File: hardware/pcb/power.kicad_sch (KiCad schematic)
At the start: 40 parts, among them J1 USB-C Port B, J2 USB-C Port A, U1 USBLC6-2SC6, U2 USBLC6-2SC6, U3 TPS2121RUX, U4 TPS22965DSG, U5 XC6206P332MR

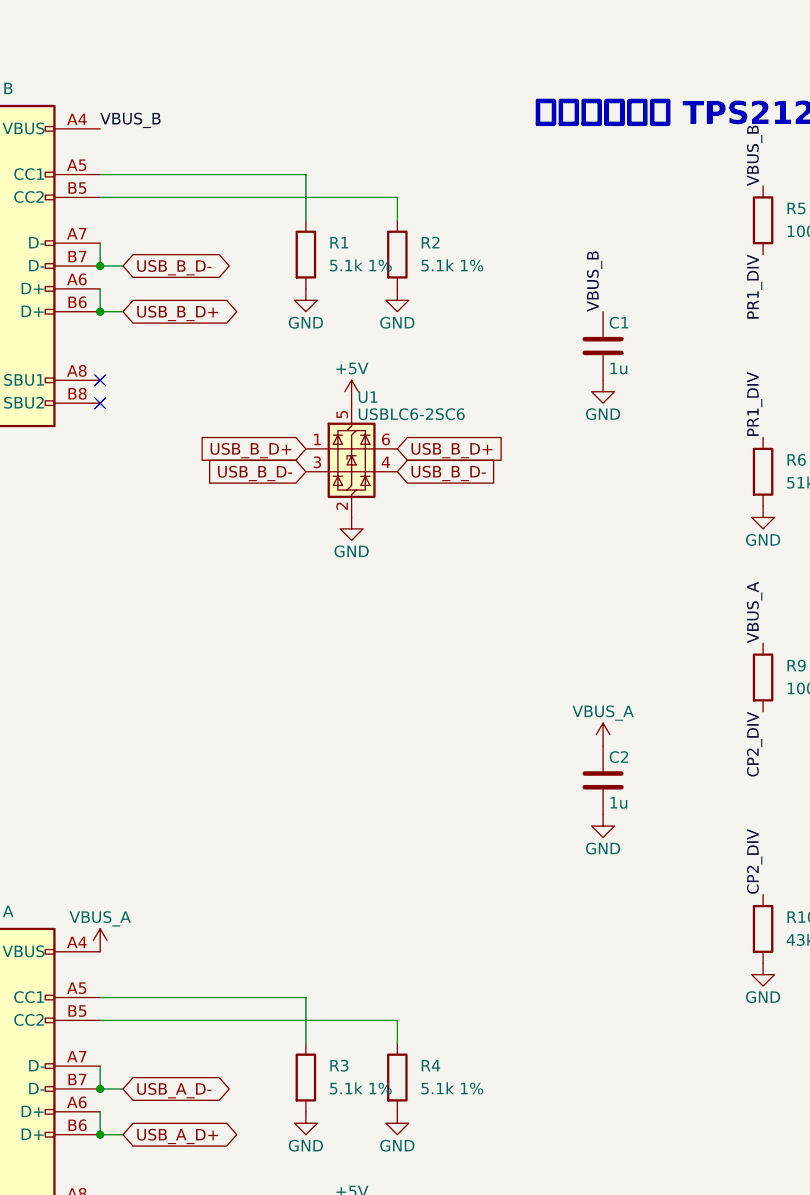
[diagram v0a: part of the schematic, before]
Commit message: Add 42-key matrix sheet, layout, and USB-C part
- Key layout from Smidr (KLE format, 42 keys) in hardware/layout,
  with the 7x6 COL2ROW matrix mapping proven on the blad keyboard
- Keymatrix sheet: 42 Choc hotswap switches and 1N4148W diodes
  (C81598, Basic), every pin labeled; RP2040 ROW/COL nets are now
  global labels, GPIO13/14 freed as spares
- USB-C receptacles J1/J2 set to HRO TYPE-C-31-M-12 (C165948)
- Power sheet: CC lines reach the RP2040 ADC again
- Docs: design decisions, pin assignment, keymatrix spec and
  reference, open items

Full project netlist matches all 141 intended nets; ERC has no errors.

Co-Authored-By: Claude Opus 5.5 <noreply@anthropic.com>
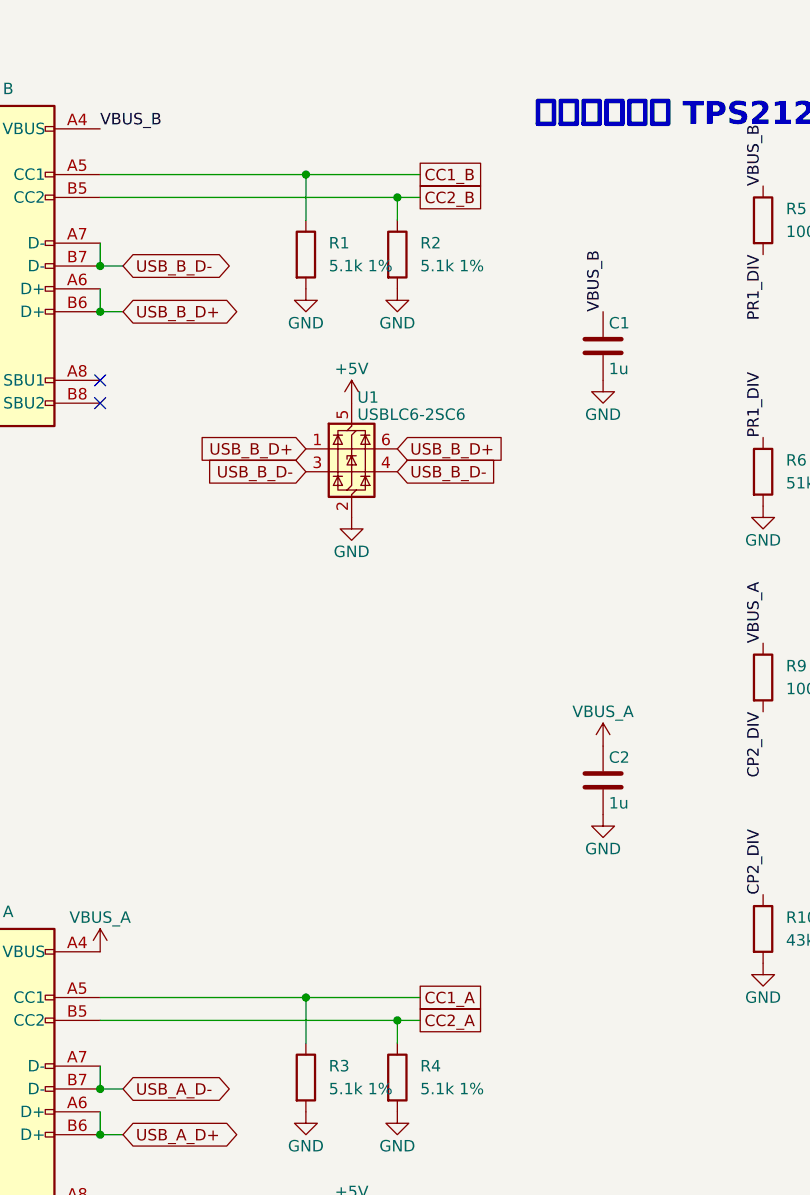
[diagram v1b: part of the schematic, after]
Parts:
- J1, J2: footprint (none) -> Connector_USB:USB_C_Receptacle_HRO_TYPE-C-31-M-12; LCSC (none) -> C165948
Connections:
- net CC2_A: now reaches J2.B5 (CC2), R4.1
- net CC1_B: now reaches J1.A5 (CC1), R1.1
- net CC2_B: now reaches J1.B5 (CC2), R2.1
- net CC1_A: now reaches J2.A5 (CC1), R3.1
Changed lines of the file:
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@@
 	)
 	(junction
+		(at 86.36 66.04)
+		(diameter 0)
+		(color 0 0 0 0)
+	)
+	(junction
 		(at 38.1 96.52)
 		(diameter 0)
@@
 	)
 	(junction
+		(at 86.36 157.48)
+		(diameter 0)
+		(color 0 0 0 0)
+	)
+	(junction
 		(at 53.34 78.74)
 		(diameter 0)
@@
 	)
 	(junction
+		(at 76.2 63.5)
+		(diameter 0)
+		(color 0 0 0 0)
+	)
+	(junction
+		(at 76.2 154.94)
+		(diameter 0)
+		(color 0 0 0 0)
+	)
+	(junction
 		(at 53.34 170.18)
 		(diameter 0)
@@
 	(wire
 		(pts
+			(xy 86.36 66.04) (xy 88.9 66.04)
+		)
+		(stroke
+			(width 0)
+			(type default)
+		)
+	)
+	(wire
+		(pts
+			(xy 76.2 63.5) (xy 88.9 63.5)
+		)
+		(stroke
+			(width 0)
+			(type default)
+		)
+	)
+	(wire
+		(pts
 			(xy 53.34 157.48) (xy 86.36 157.48)
 		)
@@
 	(wire
 		(pts
+			(xy 76.2 154.94) (xy 88.9 154.94)
+		)
+		(stroke
+			(width 0)
+			(type default)
+		)
+	)
+	(wire
+		(pts
 			(xy 53.34 63.5) (xy 76.2 63.5)
 		)
@@
 	(wire
 		(pts
+			(xy 86.36 157.48) (xy 88.9 157.48)
+		)
+		(stroke
+			(width 0)
+			(type default)
+		)
+	)
+	(wire
+		(pts
 			(xy 53.34 66.04) (xy 86.36 66.04)
 		)
@@
 		)
 	)
+	(global_label "CC1_B"
+		(shape passive)
+		(at 88.9 63.5 0)
+		(fields_autoplaced yes)
+		(effects
+			(font
+				(size 1.27 1.27)
+			)
+			(justify left)
+		)
+		(property "Intersheetrefs" "${INTERSHEET_REFS}"
+			(at 96.761 63.5 0)
+			(hide yes)
+			(show_name no)
+			(do_not_autoplace no)
+			(effects
+				(font
+					(size 1.27 1.27)
+				)
+				(justify left)
+			)
+		)
+	)
 	(global_label "USB_B_D+"
 		(shape input)
@@
 		)
 	)
+	(global_label "CC2_B"
+		(shape passive)
+		(at 88.9 66.04 0)
+		(fields_autoplaced yes)
+		(effects
+			(font
+				(size 1.27 1.27)
+			)
+			(justify left)
+		)
+		(property "Intersheetrefs" "${INTERSHEET_REFS}"
+			(at 96.761 66.04 0)
+			(hide yes)
+			(show_name no)
+			(do_not_autoplace no)
+			(effects
+				(font
+					(size 1.27 1.27)
+				)
+				(justify left)
+			)
+		)
+	)
 	(global_label "USB_A_D+"
 		(shape bidirectional)
@@
 		)
 	)
+	(global_label "CC2_A"
+		(shape passive)
+		(at 88.9 157.48 0)
+		(fields_autoplaced yes)
+		(effects
+			(font
+				(size 1.27 1.27)
+			)
+			(justify left)
+		)
+		(property "Intersheetrefs" "${INTERSHEET_REFS}"
+			(at 96.5796 157.48 0)
+			(hide yes)
+			(show_name no)
+			(do_not_autoplace no)
+			(effects
+				(font
+					(size 1.27 1.27)
+				)
+				(justify left)
+			)
+		)
+	)
 	(global_label "USB_A_D-"
 		(shape input)
@@
 		)
 	)
+	(global_label "CC1_A"
+		(shape passive)
+		(at 88.9 154.94 0)
+		(fields_autoplaced yes)
+		(effects
+			(font
+				(size 1.27 1.27)
+			)
+			(justify left)
+		)
+		(property "Intersheetrefs" "${INTERSHEET_REFS}"
+			(at 96.5796 154.94 0)
+			(hide yes)
+			(show_name no)
+			(do_not_autoplace no)
+			(effects
+				(font
+					(size 1.27 1.27)
+				)
+				(justify left)
+			)
+		)
+	)
 	(global_label "+5V_LCD"
 		(shape passive)
@@
 			)
 		)
-		(property "Footprint" ""
+		(property "Footprint" "Connector_USB:USB_C_Receptacle_HRO_TYPE-C-31-M-12"
 			(at 41.91 73.66 0)
 			(hide yes)
@@
 			)
 		)
+		(property "LCSC" "C165948"
+			(at 41.91 73.66 0)
+			(hide yes)
+			(show_name no)
+			(do_not_autoplace no)
+			(effects
+				(font
+					(size 1.27 1.27)
+				)
+			)
+		)
 		(pin "A1"
 		)
@@
 			)
 		)
-		(property "Footprint" ""
+		(property "Footprint" "Connector_USB:USB_C_Receptacle_HRO_TYPE-C-31-M-12"
 			(at 41.91 165.1 0)
 			(hide yes)
@@
 			(hide yes)
 			(show_name no)
+			(do_not_autoplace no)
+			(effects
+				(font
+					(size 1.27 1.27)
+				)
+			)
+		)
+		(property "LCSC" "C165948"
+			(at 41.91 165.1 0)
+			(hide yes)
+			(show_name no)

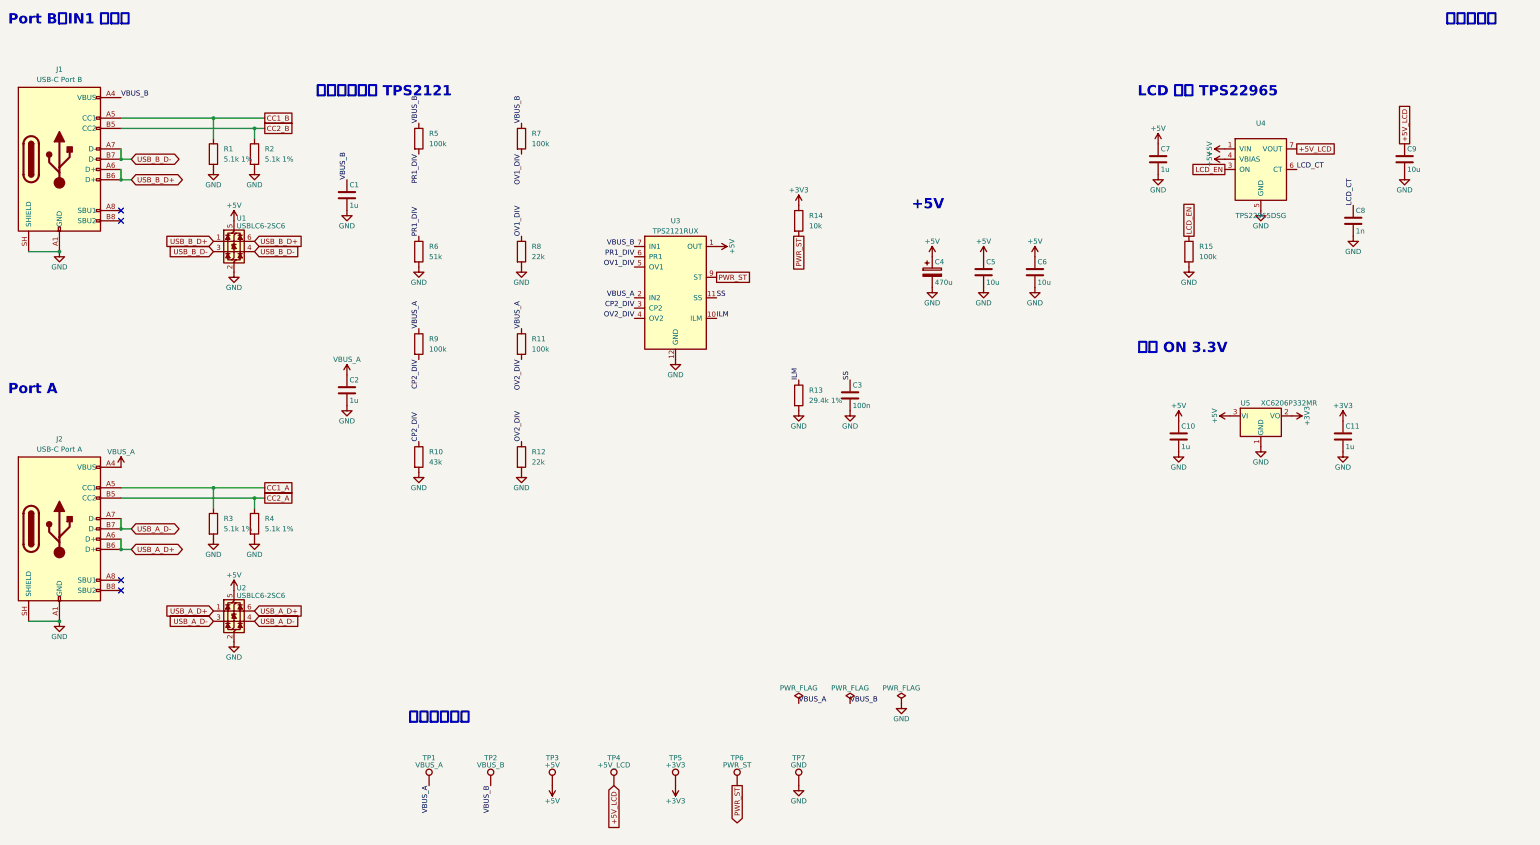
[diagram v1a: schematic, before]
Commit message: Wire the power sheet and use power symbols for +5V_LCD
Replace the labels on the power sheet with wires, use power symbols for
+5V_LCD and the VBUS test pads, and change J302 to Conn_01x03_Pin.

Co-Authored-By: Claude Opus 5.5 <noreply@anthropic.com>
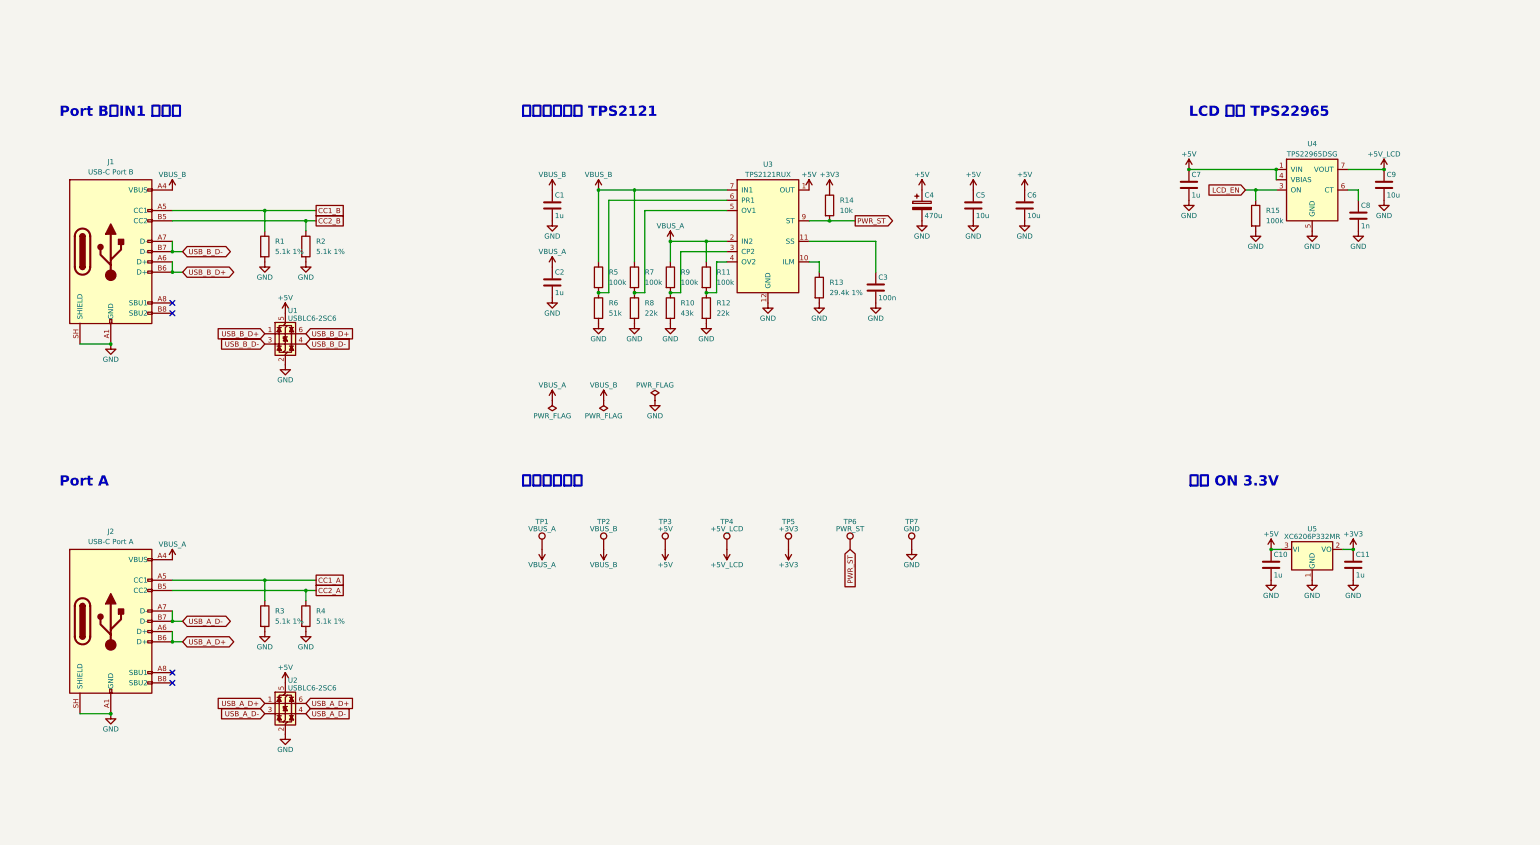
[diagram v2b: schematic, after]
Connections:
- net CP2_DIV: no longer names the net of R10.1, R9.2, U3.3 (CP2)
- net ILM: no longer names the net of R13.1, U3.10 (ILM)
- net LCD_CT: no longer names the net of C8.1, U4.6 (CT)
- net OV1_DIV: no longer names the net of R7.2, R8.1, U3.5 (OV1)
- net OV2_DIV: no longer names the net of R11.2, R12.1, U3.4 (OV2)
- net PR1_DIV: no longer names the net of R5.2, R6.1, U3.6 (PR1)
- net SS: no longer names the net of C3.1, U3.11 (SS)
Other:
- note removed: "+5V"
- note removed: "シート外へ"
- moved on the sheet: C1, C10, C11, C2, C3, C4, C5, C6, C7, C8, C9, J1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

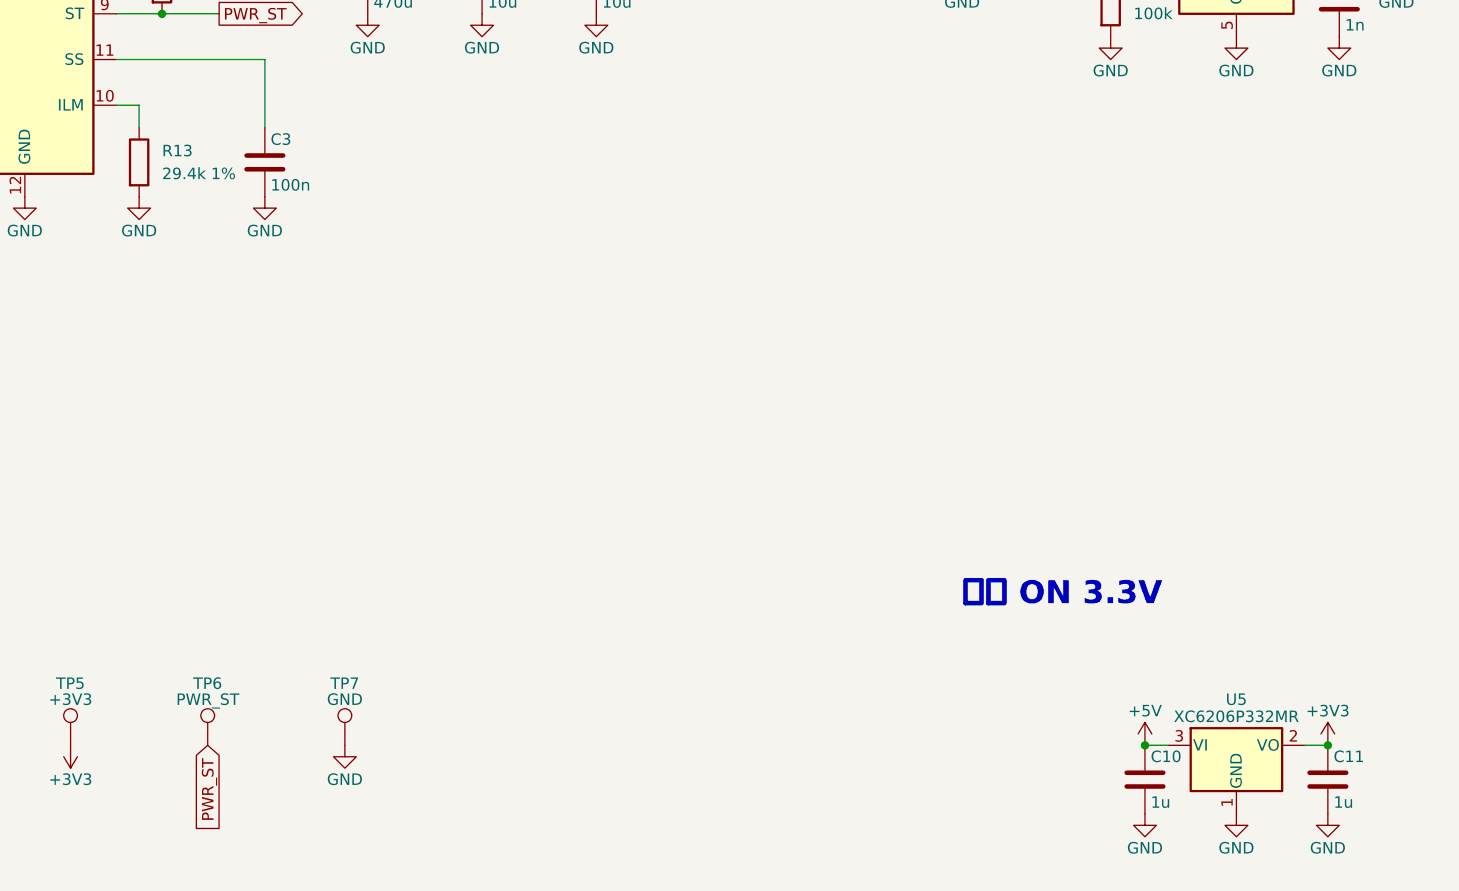
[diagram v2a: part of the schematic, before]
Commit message: Assign 0603 parts, use 30k for ILM, and switch the LDO to AP2127
Give every resistor and capacitor a 0603 footprint and an LCSC number
(Basic where possible), change the ILM resistor to a 30k Basic part,
and replace the XC6206 with an AP2127N-3.3 from stock. Record the
decisions and drop the resolved open items.

Co-Authored-By: Claude Opus 5.5 <noreply@anthropic.com>
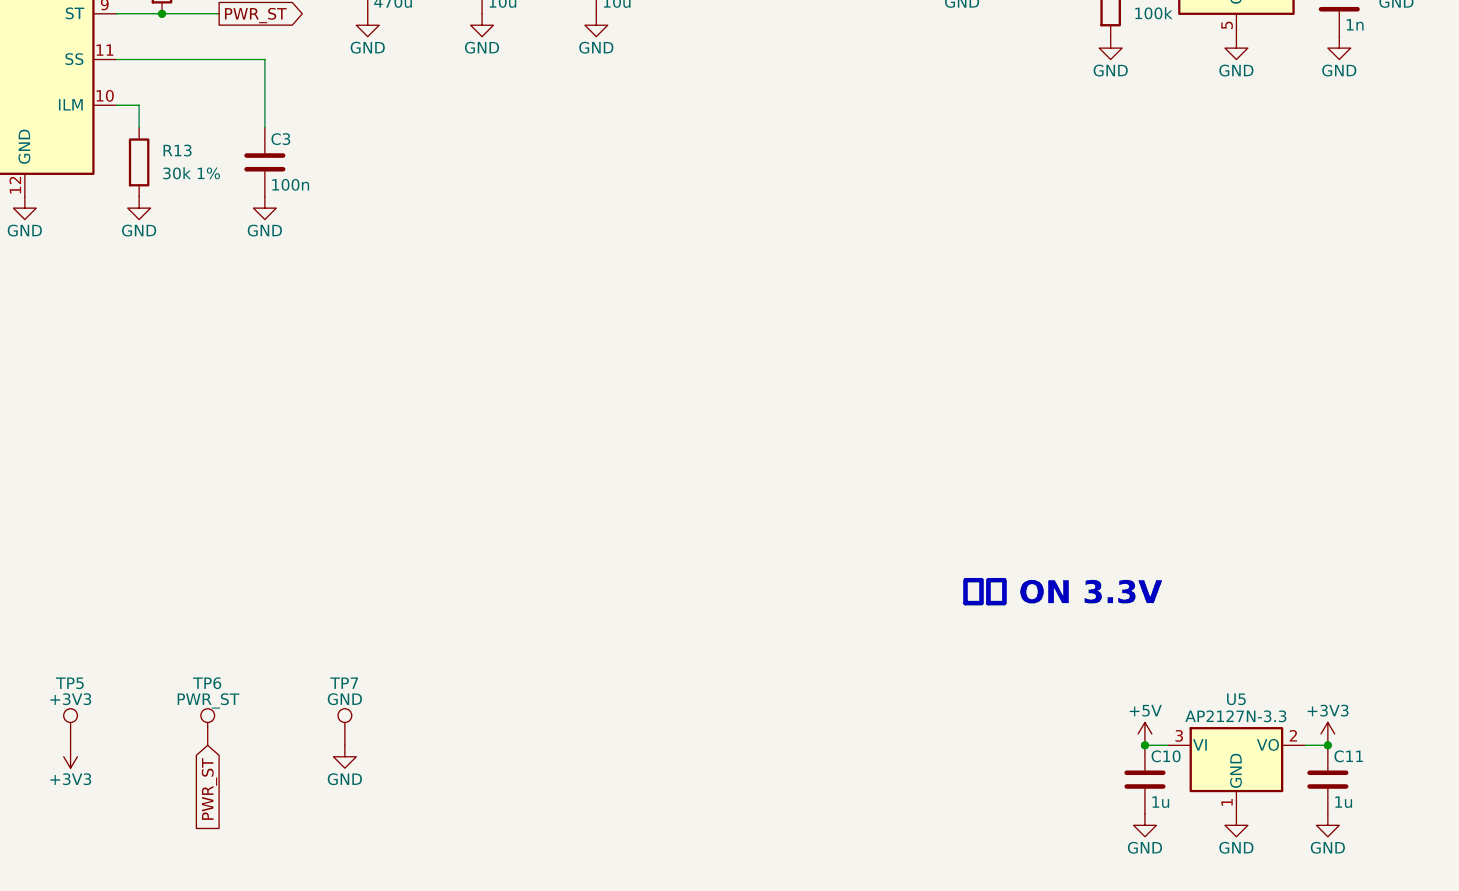
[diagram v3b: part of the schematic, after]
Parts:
- C1, C10, C11, C2, C7: footprint (none) -> Capacitor_SMD:C_0603_1608Metric; LCSC (none) -> C15849
- C3: footprint (none) -> Capacitor_SMD:C_0603_1608Metric; LCSC (none) -> C14663
- C5, C6, C9: footprint (none) -> Capacitor_SMD:C_0603_1608Metric; LCSC (none) -> C96446
- C8: footprint (none) -> Capacitor_SMD:C_0603_1608Metric; LCSC (none) -> C1588
- R1, R2, R3, R4: footprint (none) -> Resistor_SMD:R_0603_1608Metric; LCSC (none) -> C23186
- R10: footprint (none) -> Resistor_SMD:R_0603_1608Metric; LCSC (none) -> C23172
- R11, R15, R5, R7, R9: footprint (none) -> Resistor_SMD:R_0603_1608Metric; LCSC (none) -> C25803
- R12, R8: footprint (none) -> Resistor_SMD:R_0603_1608Metric; LCSC (none) -> C31850
- R13: value 29.4k 1% -> 30k 1%; footprint (none) -> Resistor_SMD:R_0603_1608Metric; LCSC (none) -> C22984
- R14: footprint (none) -> Resistor_SMD:R_0603_1608Metric; LCSC (none) -> C25804
- R6: footprint (none) -> Resistor_SMD:R_0603_1608Metric; LCSC (none) -> C23196
- U5: value XC6206P332MR -> AP2127N-3.3; symbol Regulator_Linear:XC6206PxxxMR -> Regulator_Linear:AP2127N-3.3; LCSC C5446 -> C176954
